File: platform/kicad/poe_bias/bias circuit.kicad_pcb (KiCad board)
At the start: 2 copper layers, 35.5 x 33 mm, 10 parts, among them J1 Screw_Terminal_01x06, J2 Screw_Terminal_01x06

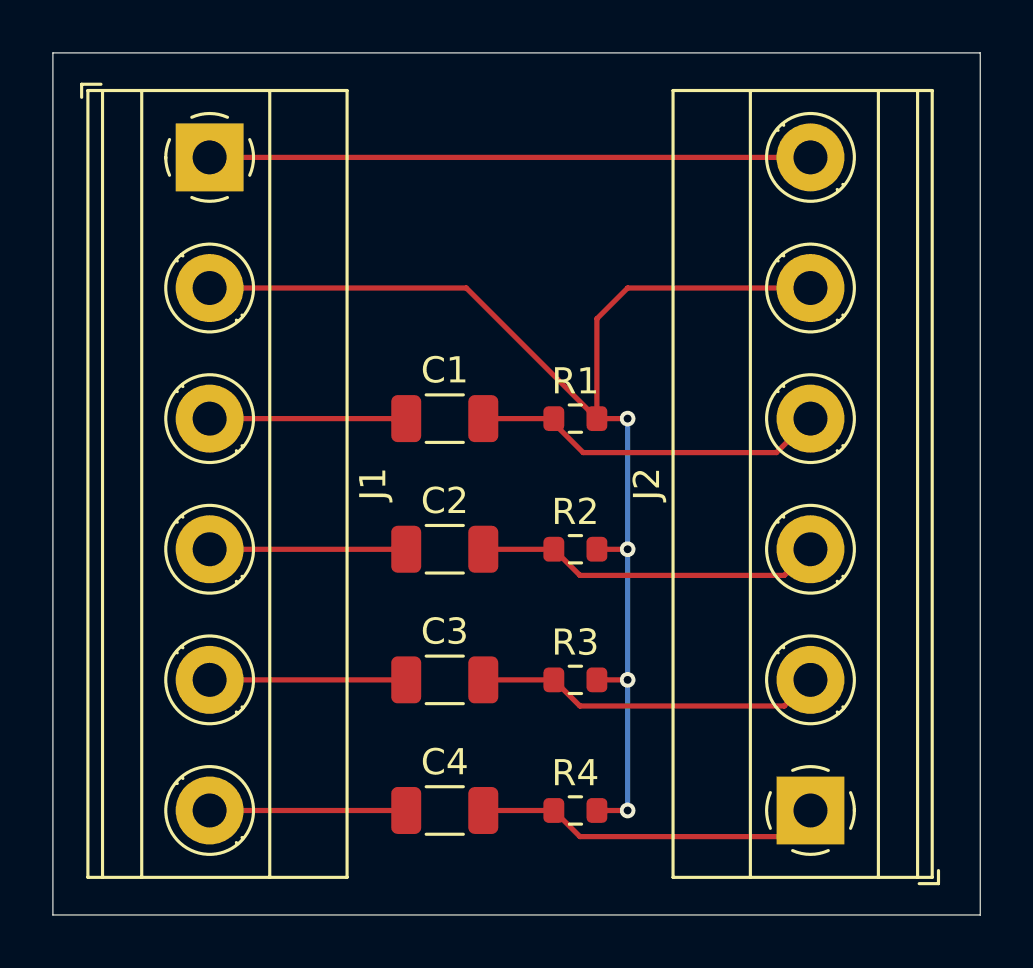
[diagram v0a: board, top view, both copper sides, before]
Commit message: PoE Bias: Update PCB layout
This change shrinks the profile of the PCB, as well as adding mounting holes and labelling.
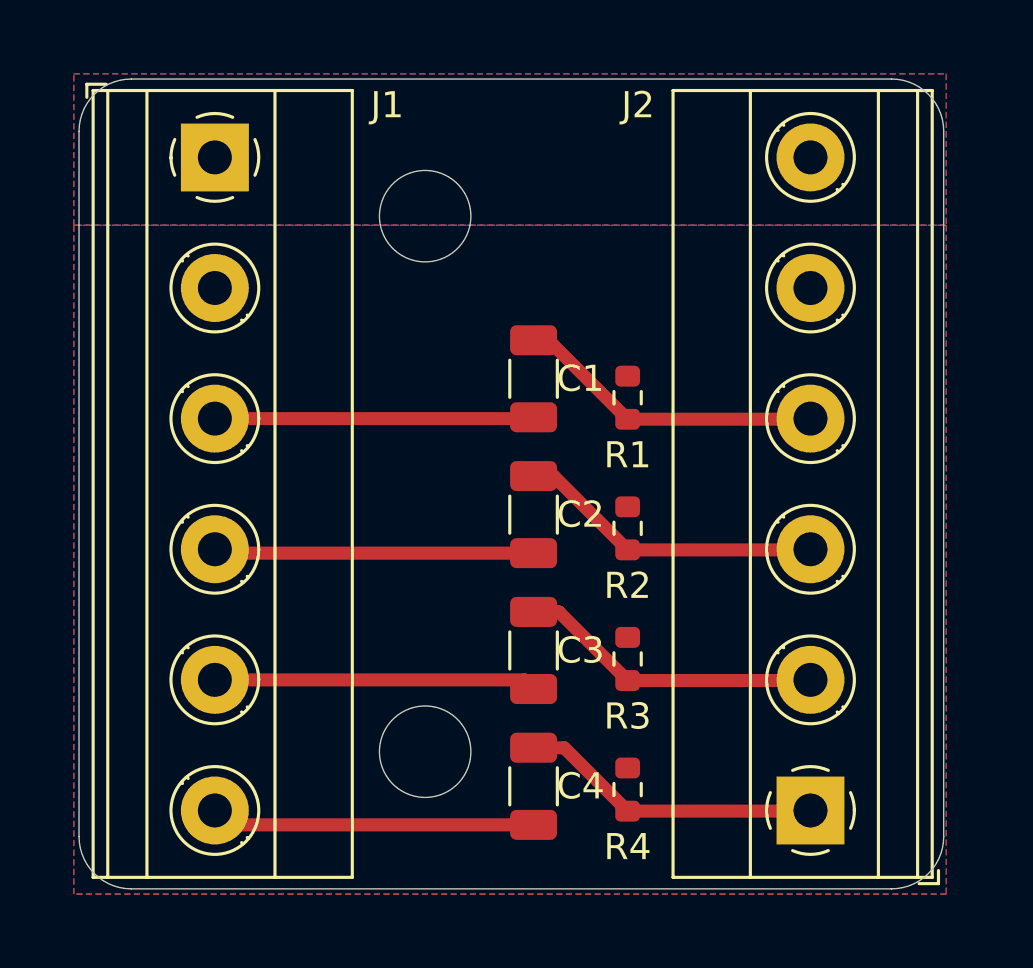
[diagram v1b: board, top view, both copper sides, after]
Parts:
- moved C1 3.73 mm to (137.4, 93.5), turned to 90 degrees
- moved C2 3.65 mm to (137.4, 98.7), turned to 90 degrees
- moved C3 3.58 mm to (137.4, 103.9), turned to 90 degrees
- moved C4 3.52 mm to (137.4, 109.1), turned to 90 degrees
- moved R1 2.15 mm to (141.0, 94.2), turned to 90 degrees
- moved R2 2.15 mm to (141.0, 99.2), turned to 90 degrees
- moved R3 2.15 mm to (141.0, 104.2), turned to 90 degrees
- moved R4 2.15 mm to (141.0, 109.2), turned to 90 degrees
- moved J1 0.20 mm to (125.2, 85.0)
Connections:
- net Net-(J1-Pin_1) renamed GND
- net Net-(J1-Pin_2) renamed +24V
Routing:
- net +24V: track 49.1 -> 0.00 mm, vias 4 -> 0
- net GND: track 23.0 -> 0.00 mm
- net Net-(J1-Pin_6): track 7.53 -> 12.4 mm
- net Net-(J1-Pin_5): track 7.53 -> 12.3 mm
- net Net-(J1-Pin_4): track 7.53 -> 12.3 mm
- net Net-(J1-Pin_3): track 7.53 -> 12.2 mm
- net Net-(J2-Pin_4): track 13.7 -> 11.9 mm
- net Net-(J2-Pin_1): track 13.4 -> 11.6 mm
- net Net-(J2-Pin_2): track 13.4 -> 11.7 mm
- net Net-(J2-Pin_3): track 13.4 -> 11.8 mm
- added copper zone on B.Cu, net +24V
- added copper zone on F.Cu, net +24V
- added copper zone on B.Cu, net GND
- added copper zone on F.Cu, net GND
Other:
- board size 35.5 x 33 mm -> 33.1 x 31 mm
